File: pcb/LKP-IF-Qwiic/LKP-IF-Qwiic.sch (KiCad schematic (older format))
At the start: 7 parts, among them J1 JST SH, J2 JST SH, J3 LKP SWD .1\" Extra Long, J4 LKP I/O .1\" Extra Long, U1 TCA9406DCTR

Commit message: LKP-IF-Qwiic: Add board.
LKP-Core: Add more measurements.
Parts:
- J1, J2: footprint Connector_JST:JST_SH_BM04B-SRSS-TB_1x04-1MP_P1.00mm_Vertical -> Connector_JST:JST_SH_SM04B-SRSS-TB_1x04-1MP_P1.00mm_Horizontal
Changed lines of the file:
@@
 encoding utf-8
 Sheet 1 1
-Title ""
-Date ""
+Title "LKP-IF-Qwiic"
+Date "2021-03-01"
 Rev ""
-Comp ""
+Comp "dogtopus"
 Comment1 ""
 Comment2 ""
@@
 F 0 "J2" H 4478 4326 50  0000 L CNN
 F 1 "JST SH" H 4478 4233 50  0000 L CNN
-F 2 "Connector_JST:JST_SH_BM04B-SRSS-TB_1x04-1MP_P1.00mm_Vertical" H 4450 4350 50  0001 C CNN
+F 2 "Connector_JST:JST_SH_SM04B-SRSS-TB_1x04-1MP_P1.00mm_Horizontal" H 4450 4350 50  0001 C CNN
 F 3 "~" H 4450 4350 50  0001 C CNN
 	1    4450 4350
@@
 F 0 "J1" H 4478 3626 50  0000 L CNN
 F 1 "JST SH" H 4478 3533 50  0000 L CNN
-F 2 "Connector_JST:JST_SH_BM04B-SRSS-TB_1x04-1MP_P1.00mm_Vertical" H 4450 3650 50  0001 C CNN
+F 2 "Connector_JST:JST_SH_SM04B-SRSS-TB_1x04-1MP_P1.00mm_Horizontal" H 4450 3650 50  0001 C CNN
 F 3 "~" H 4450 3650 50  0001 C CNN
 	1    4450 3650
@@
 	4150 3550 4250 3550
 Wire Wire Line
-	4250 3650 4150 3650
+	4250 3650 4200 3650
 $Comp
 L power:+3V3 #PWR0103
@@
 $EndComp
 Wire Wire Line
-	4150 4250 4250 4250
-Wire Wire Line
 	4250 4350 4150 4350
 Text Label 3950 3750 0    50   ~ 0
@@
 NoConn ~ 7100 4000
 Wire Wire Line
-	7000 3600 7100 3600
+	7000 3600 7050 3600
 Wire Wire Line
 	7100 3700 7000 3700
@@
 Wire Wire Line
 	6250 3950 6250 3850
+$Comp
+L power:PWR_FLAG #FLG0101
+U 1 1 604022BA
+P 4200 3400
+F 0 "#FLG0101" H 4200 3475 50  0001 C CNN
+F 1 "PWR_FLAG" H 4200 3576 50  0000 C CNN
+F 2 "" H 4200 3400 50  0001 C CNN
+F 3 "~" H 4200 3400 50  0001 C CNN
+	1    4200 3400
+	1    0    0    -1
+$EndComp
+Wire Wire Line
+	4200 3400 4200 3650
+Connection ~ 4200 3650
+Wire Wire Line
+	4200 3650 4150 3650
+$Comp
+L power:PWR_FLAG #FLG0102
+U 1 1 60403C98
+P 7050 3550
+F 0 "#FLG0102" H 7050 3625 50  0001 C CNN
+F 1 "PWR_FLAG" H 7050 3726 50  0000 C CNN
+F 2 "" H 7050 3550 50  0001 C CNN
+F 3 "~" H 7050 3550 50  0001 C CNN
+	1    7050 3550
+	1    0    0    -1
+$EndComp
+Wire Wire Line
+	7050 3550 7050 3600
+Connection ~ 7050 3600
+Wire Wire Line
+	7050 3600 7100 3600
+$Comp
+L power:PWR_FLAG #FLG0103
+U 1 1 604072A7
+P 4250 3450
+F 0 "#FLG0103" H 4250 3525 50  0001 C CNN
+F 1 "PWR_FLAG" V 4250 3580 50  0000 L CNN
+F 2 "" H 4250 3450 50  0001 C CNN
+F 3 "~" H 4250 3450 50  0001 C CNN
+	1    4250 3450
+	0    1    1    0
+$EndComp
+Wire Wire Line
+	4250 3550 4250 3450
+Connection ~ 4250 3550
+Wire Wire Line
+	4150 4250 4250 4250
 $EndSCHEMATC

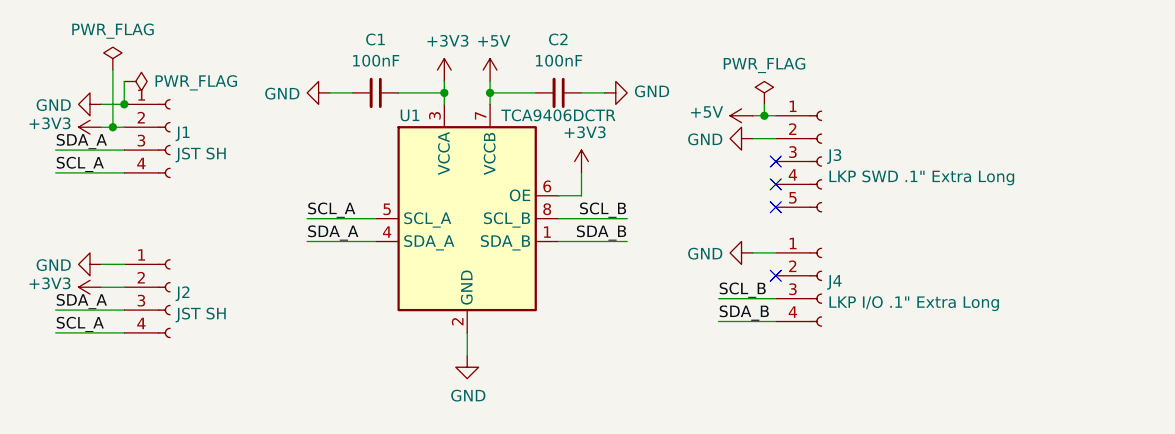
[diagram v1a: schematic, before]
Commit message: LKP-IF-Qwiic: Add reverse voltage protection.
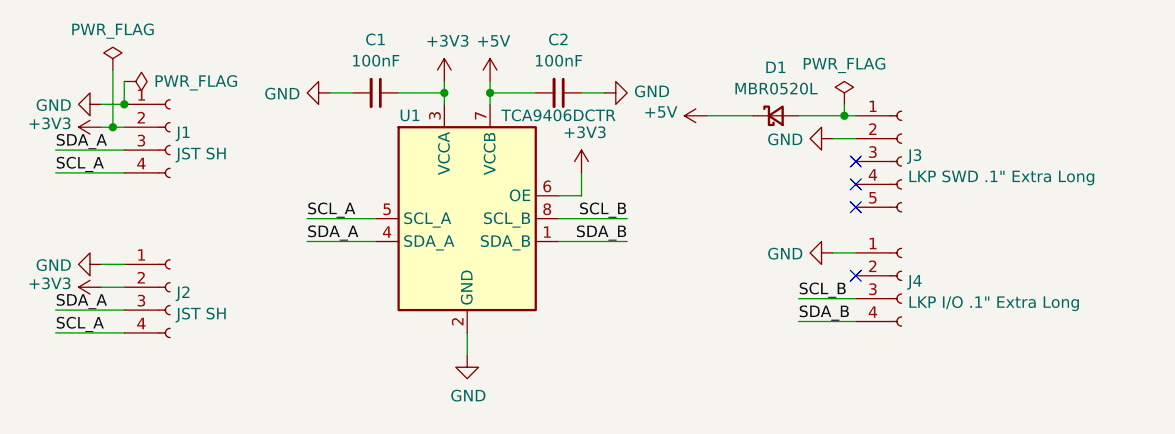
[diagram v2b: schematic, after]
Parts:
- added D1: MBR0520L, Diode_SMD:D_SOD-123, symbol Device:D_Schottky_Small
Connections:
- net +5V: now also D1.1 (K); no longer J3.1 (Pin_1)
- new net: D1.2 (A), J3.1 (Pin_1)
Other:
- moved on the sheet: J3, J4
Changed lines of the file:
@@
 L Connector:Conn_01x05_Female J3
 U 1 1 603DDC64
-P 7300 3800
-F 0 "J3" H 7328 3826 50  0000 L CNN
-F 1 "LKP SWD .1\" Extra Long" H 7328 3733 50  0000 L CNN
-F 2 "Connector_PinSocket_2.54mm:PinSocket_1x05_P2.54mm_Vertical" H 7300 3800 50  0001 C CNN
-F 3 "~" H 7300 3800 50  0001 C CNN
-	1    7300 3800
+P 7650 3800
+F 0 "J3" H 7678 3826 50  0000 L CNN
+F 1 "LKP SWD .1\" Extra Long" H 7678 3733 50  0000 L CNN
+F 2 "Connector_PinSocket_2.54mm:PinSocket_1x05_P2.54mm_Vertical" H 7650 3800 50  0001 C CNN
+F 3 "~" H 7650 3800 50  0001 C CNN
+	1    7650 3800
 	1    0    0    -1
 $EndComp
@@
 L power:+5V #PWR0109
 U 1 1 603DE36D
-P 7000 3600
-F 0 "#PWR0109" H 7000 3450 50  0001 C CNN
-F 1 "+5V" V 7015 3730 50  0000 L CNN
-F 2 "" H 7000 3600 50  0001 C CNN
-F 3 "" H 7000 3600 50  0001 C CNN
-	1    7000 3600
+P 6800 3600
+F 0 "#PWR0109" H 6800 3450 50  0001 C CNN
+F 1 "+5V" V 6815 3730 50  0000 L CNN
+F 2 "" H 6800 3600 50  0001 C CNN
+F 3 "" H 6800 3600 50  0001 C CNN
+	1    6800 3600
 	0    -1   -1   0
 $EndComp
@@
 L power:GND #PWR0110
 U 1 1 603DE9FB
-P 7000 3700
-F 0 "#PWR0110" H 7000 3450 50  0001 C CNN
-F 1 "GND" V 7005 3570 50  0000 R CNN
-F 2 "" H 7000 3700 50  0001 C CNN
-F 3 "" H 7000 3700 50  0001 C CNN
-	1    7000 3700
+P 7350 3700
+F 0 "#PWR0110" H 7350 3450 50  0001 C CNN
+F 1 "GND" V 7355 3570 50  0000 R CNN
+F 2 "" H 7350 3700 50  0001 C CNN
+F 3 "" H 7350 3700 50  0001 C CNN
+	1    7350 3700
 	0    1    1    0
 $EndComp
-NoConn ~ 7100 3800
-NoConn ~ 7100 3900
-NoConn ~ 7100 4000
+NoConn ~ 7450 3800
+NoConn ~ 7450 3900
+NoConn ~ 7450 4000
 Wire Wire Line
-	7000 3600 7050 3600
-Wire Wire Line
-	7100 3700 7000 3700
+	7450 3700 7350 3700
 $Comp
 L Connector:Conn_01x04_Female J4
 U 1 1 603DFE23
-P 7300 4300
-F 0 "J4" H 7328 4276 50  0000 L CNN
-F 1 "LKP I/O .1\" Extra Long" H 7328 4183 50  0000 L CNN
-F 2 "Connector_PinSocket_2.54mm:PinSocket_1x04_P2.54mm_Vertical" H 7300 4300 50  0001 C CNN
-F 3 "~" H 7300 4300 50  0001 C CNN
-	1    7300 4300
+P 7650 4300
+F 0 "J4" H 7678 4276 50  0000 L CNN
+F 1 "LKP I/O .1\" Extra Long" H 7678 4183 50  0000 L CNN
+F 2 "Connector_PinSocket_2.54mm:PinSocket_1x04_P2.54mm_Vertical" H 7650 4300 50  0001 C CNN
+F 3 "~" H 7650 4300 50  0001 C CNN
+	1    7650 4300
 	1    0    0    -1
 $EndComp
@@
 L power:GND #PWR0111
 U 1 1 603E08C5
-P 7000 4200
-F 0 "#PWR0111" H 7000 3950 50  0001 C CNN
-F 1 "GND" V 7005 4070 50  0000 R CNN
-F 2 "" H 7000 4200 50  0001 C CNN
-F 3 "" H 7000 4200 50  0001 C CNN
-	1    7000 4200
+P 7350 4200
+F 0 "#PWR0111" H 7350 3950 50  0001 C CNN
+F 1 "GND" V 7355 4070 50  0000 R CNN
+F 2 "" H 7350 4200 50  0001 C CNN
+F 3 "" H 7350 4200 50  0001 C CNN
+	1    7350 4200
 	0    1    1    0
 $EndComp
 Wire Wire Line
-	7100 4200 7000 4200
-NoConn ~ 7100 4300
+	7450 4200 7350 4200
+NoConn ~ 7450 4300
 Wire Wire Line
-	6850 4400 7100 4400
-Text Label 6850 4500 0    50   ~ 0
+	7200 4400 7450 4400
+Text Label 7200 4500 0    50   ~ 0
 SDA_B
-Text Label 6850 4400 0    50   ~ 0
+Text Label 7200 4400 0    50   ~ 0
 SCL_B
 Wire Wire Line
-	7100 4500 6850 4500
+	7450 4500 7200 4500
 Text Label 6450 4150 2    50   ~ 0
 SDA_B
@@
 L power:PWR_FLAG #FLG0102
 U 1 1 60403C98
-P 7050 3550
-F 0 "#FLG0102" H 7050 3625 50  0001 C CNN
-F 1 "PWR_FLAG" H 7050 3726 50  0000 C CNN
-F 2 "" H 7050 3550 50  0001 C CNN
-F 3 "~" H 7050 3550 50  0001 C CNN
-	1    7050 3550
+P 7400 3550
+F 0 "#FLG0102" H 7400 3625 50  0001 C CNN
+F 1 "PWR_FLAG" H 7400 3726 50  0000 C CNN
+F 2 "" H 7400 3550 50  0001 C CNN
+F 3 "~" H 7400 3550 50  0001 C CNN
+	1    7400 3550
 	1    0    0    -1
 $EndComp
 Wire Wire Line
-	7050 3550 7050 3600
-Connection ~ 7050 3600
+	7400 3550 7400 3600
+Connection ~ 7400 3600
 Wire Wire Line
-	7050 3600 7100 3600
+	7400 3600 7450 3600
 $Comp
 L power:PWR_FLAG #FLG0103
@@
 Wire Wire Line
 	4150 4250 4250 4250
+Wire Wire Line
+	6800 3600 7000 3600
+Wire Wire Line
+	7200 3600 7400 3600
+$Comp
+L Device:D_Schottky_Small D1
+U 1 1 603F9569
+P 7100 3600
+F 0 "D1" H 7100 3810 50  0000 C CNN
+F 1 "MBR0520L" H 7100 3717 50  0000 C CNN
+F 2 "Diode_SMD:D_SOD-123" V 7100 3600 50  0001 C CNN
+F 3 "~" V 7100 3600 50  0001 C CNN
+	1    7100 3600
+	1    0    0    -1
+$EndComp
 $EndSCHEMATC

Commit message: LKP-IF-Qwiic: Add INT passthrough connector as an alternative to stacking headers.
README: Add notes about how to find the hard-to-find 18-pin male header.
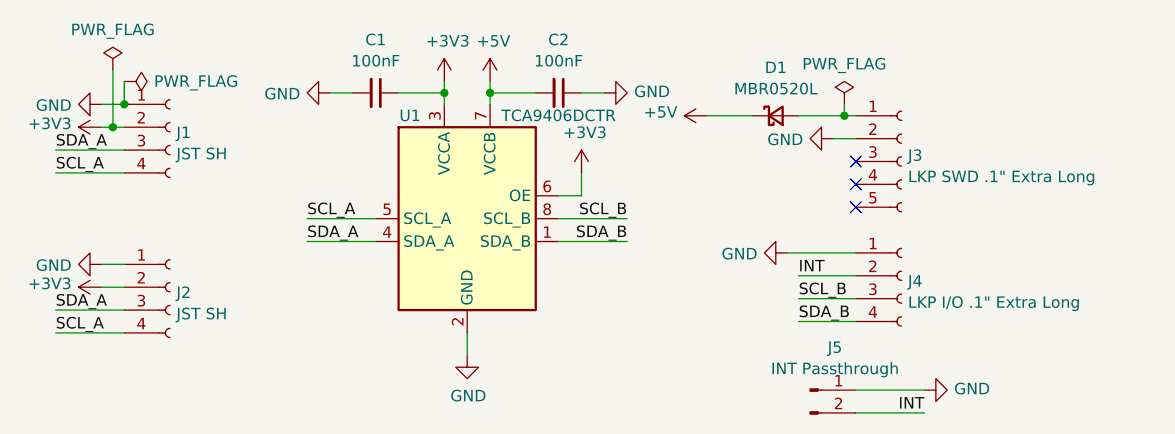
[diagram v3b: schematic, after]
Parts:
- added J5: INT Passthrough, Connector_PinHeader_2.54mm:PinHeader_1x02_P2.54mm_Vertical, symbol Connector:Conn_01x02_Male
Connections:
- net GND: now also J5.1 (Pin_1)
- net INT: now reaches J4.2 (Pin_2)
- net INT: now also J5.2 (Pin_2)
- no-connect marks 4 -> 3
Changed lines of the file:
@@
 L power:GND #PWR0111
 U 1 1 603E08C5
-P 7350 4200
-F 0 "#PWR0111" H 7350 3950 50  0001 C CNN
-F 1 "GND" V 7355 4070 50  0000 R CNN
-F 2 "" H 7350 4200 50  0001 C CNN
-F 3 "" H 7350 4200 50  0001 C CNN
-	1    7350 4200
+P 7150 4200
+F 0 "#PWR0111" H 7150 3950 50  0001 C CNN
+F 1 "GND" V 7155 4070 50  0000 R CNN
+F 2 "" H 7150 4200 50  0001 C CNN
+F 3 "" H 7150 4200 50  0001 C CNN
+	1    7150 4200
 	0    1    1    0
 $EndComp
-Wire Wire Line
-	7450 4200 7350 4200
-NoConn ~ 7450 4300
 Wire Wire Line
 	7200 4400 7450 4400
@@
 	1    0    0    -1
 $EndComp
+$Comp
+L Connector:Conn_01x02_Male J5
+U 1 1 6040C021
+P 7250 4800
+F 0 "J5" H 7359 4986 50  0000 C CNN
+F 1 "INT Passthrough" H 7359 4893 50  0000 C CNN
+F 2 "Connector_PinHeader_2.54mm:PinHeader_1x02_P2.54mm_Vertical" H 7250 4800 50  0001 C CNN
+F 3 "~" H 7250 4800 50  0001 C CNN
+	1    7250 4800
+	1    0    0    -1
+$EndComp
+$Comp
+L power:GND #PWR0114
+U 1 1 6040CF1F
+P 7750 4800
+F 0 "#PWR0114" H 7750 4550 50  0001 C CNN
+F 1 "GND" V 7755 4670 50  0000 R CNN
+F 2 "" H 7750 4800 50  0001 C CNN
+F 3 "" H 7750 4800 50  0001 C CNN
+	1    7750 4800
+	0    -1   -1   0
+$EndComp
+Wire Wire Line
+	7450 4800 7750 4800
+Text Label 7750 4900 2    50   ~ 0
+INT
+Text Label 7200 4300 0    50   ~ 0
+INT
+Wire Wire Line
+	7200 4300 7450 4300
+Wire Wire Line
+	7150 4200 7450 4200
+Wire Wire Line
+	7750 4900 7450 4900
 $EndSCHEMATC
